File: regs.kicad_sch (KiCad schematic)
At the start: 1 part, among them U17 3-641215-6

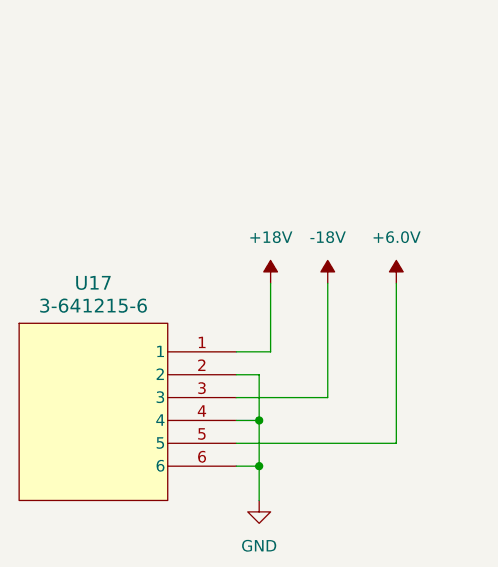
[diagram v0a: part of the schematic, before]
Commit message: Add all 4 channels
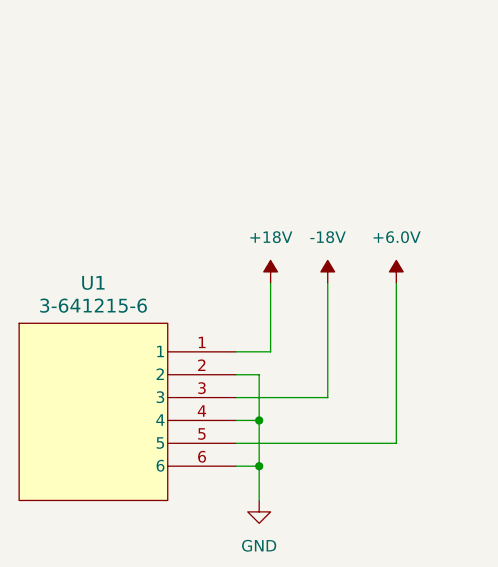
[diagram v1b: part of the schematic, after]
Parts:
- renumbered U17 to U1
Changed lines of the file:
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@@
 		(dnp no)
 		(fields_autoplaced yes)
-		(property "Reference" "#PWR0140"
+		(property "Reference" "#PWR012"
 			(at 58.42 80.01 0)
 			(effects
@@
 			(project "psc_carrier_brd"
 				(path "/40891cc8-bf64-41f4-8f69-a607d7b280eb/d1842e08-6ad7-4891-bdb3-3a3a498e2a30"
-					(reference "#PWR0140")
+					(reference "#PWR012")
 					(unit 1)
 				)
@@
 		(dnp no)
 		(fields_autoplaced yes)
-		(property "Reference" "#PWR0141"
+		(property "Reference" "#PWR013"
 			(at 66.04 80.01 0)
 			(effects
@@
 			(project ""
 				(path "/40891cc8-bf64-41f4-8f69-a607d7b280eb/d1842e08-6ad7-4891-bdb3-3a3a498e2a30"
-					(reference "#PWR0141")
+					(reference "#PWR013")
 					(unit 1)
 				)
@@
 		(dnp no)
 		(fields_autoplaced yes)
-		(property "Reference" "U17"
+		(property "Reference" "U1"
 			(at 32.385 76.2 0)
 			(effects
@@
 			(project ""
 				(path "/40891cc8-bf64-41f4-8f69-a607d7b280eb/d1842e08-6ad7-4891-bdb3-3a3a498e2a30"
-					(reference "U17")
+					(reference "U1")
 					(unit 1)
 				)
@@
 		(dnp no)
 		(fields_autoplaced yes)
-		(property "Reference" "#PWR0142"
+		(property "Reference" "#PWR010"
 			(at 50.8 106.68 0)
 			(effects
@@
 			(project ""
 				(path "/40891cc8-bf64-41f4-8f69-a607d7b280eb/d1842e08-6ad7-4891-bdb3-3a3a498e2a30"
-					(reference "#PWR0142")
+					(reference "#PWR010")
 					(unit 1)
 				)
@@
 		(dnp no)
 		(fields_autoplaced yes)
-		(property "Reference" "#PWR0139"
+		(property "Reference" "#PWR011"
 			(at 52.07 80.01 0)
 			(effects
@@
 			(project "psc_carrier_brd"
 				(path "/40891cc8-bf64-41f4-8f69-a607d7b280eb/d1842e08-6ad7-4891-bdb3-3a3a498e2a30"
-					(reference "#PWR0139")
-					(unit 1)
-				)
+					(reference "#PWR011")
+					(unit 1)
+				)

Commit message: Start routing
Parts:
- added J4: 39301022, myparts:MOLEX_39301022, symbol psc:39301022
- added R68, R69: 10K, Resistor_SMD:R_0402_1005Metric, symbol Device:R_US
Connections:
- net +6.0V is gone; now on net GND: U1.5
- net GND: now also J4.2
- net i2c_scl: now also R68.2
- net i2c_sda: now also R69.2
- new net +3.3V: R68.1, R69.1
- new net +5.0V: J4.1
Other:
- sheet +15v -15v DCCT Regulators: file regs_15v.kicad_sch -> regs_dcct_15v.kicad_sch
- sheet +5VD regulator ports: added none; removed imon_hi, imon_lo
- sheet vi_monitor ports: added none; removed mon1_v1, mon1_v2
- note added: "Input Power Connector"
- note added: "Output Power Connector (To zuDFE)"
- moved on the sheet: U1

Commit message: Finished layout
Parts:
- added D3: GREEN, LED_SMD:LED_0603_1608Metric, symbol Device:LED
- added R70: 10K, Resistor_SMD:R_0402_1005Metric, symbol Device:R_US
- added R71: 160, Resistor_SMD:R_0402_1005Metric, symbol Device:R_US
- added TP18, TP19: ${SHORT_NET_NAME(1)}, myparts:TestPoint_RCS-0C, symbol Connector:TestPoint
- J4: Cost (none) -> 1.25; MFG (none) -> Molex; MFG_PN (none) -> 0039301022
- R68, R69: Cost (none) -> 0.01; MFG (none) -> Panasonic; MFG_PN (none) -> ERJ-2RKF1002X
- U1: Cost (none) -> 1.78; MFG (none) -> TE; MFG_PN (none) -> 3-641215-6
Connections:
- net GND: now also D3.1 (K), R70.2
- net i2c_scl: now also TP18.1
- net i2c_sda: now also TP19.1
- new net: D3.2 (A), R71.2
- new net enb: R70.1, R71.1
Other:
- sheet +1.8V regulator ports: added enb; removed none
- sheet +2.5V regulator ports: added enb; removed none
- sheet +3.3V regulator ports: added enb; removed none
- moved on the sheet: R69
